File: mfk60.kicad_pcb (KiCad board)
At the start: 2 copper layers, 300 x 95.2 mm, 181 parts, among them J1 USB_C_Receptacle_USB2.0, J2 TRRS Jack, J3 ISP, J4 USB_C_Receptacle_USB2.0, J5 TRRS Jack, J6 ISP, SW1 KS-33, SW10 KS-33, SW11 KS-33, SW12 KS-33, SW13 KS-33, SW14 KS-33, SW15 KS-33, SW16 KS-33, SW17 KS-33, SW18 KS-33, SW19 KS-33, SW2 KS-33, SW20 KS-33, SW21 KS-33, SW22 KS-33, SW23 KS-33, SW24 KS-33, SW25 KS-33, SW26 KS-33, SW27 KS-33, SW28 KS-33, SW29 KS-33, SW3 KS-33, SW30 KS-33, SW31 KS-33, SW32 KS-33, SW33 KS-33, SW34 KS-33, SW35 KS-33, SW36 KS-33, SW37 KS-33, SW38 KS-33, SW39 KS-33, SW4 KS-33, SW40 KS-33, SW41 KS-33, SW42 KS-33, SW43 KS-33, SW44 KS-33, SW45 KS-33, SW46 KS-33, SW47 KS-33, SW48 KS-33, SW49 KS-33, SW5 KS-33, SW50 KS-33, SW51 KS-33, SW52 KS-33, SW53 KS-33, SW54 KS-33, SW55 KS-33, SW56 KS-33, SW57 KS-33, SW58 KS-33, SW59 KS-33, SW6 KS-33, SW60 KS-33, SW61 KS-33, SW62 RST, SW63 RST, SW7 KS-33, SW8 KS-33, SW9 KS-33, T1 Tab, T2 Tab, T3 Tab, T4 Tab, T5 Tab, T6 Tab, T7 Tab, U1 ATmega32U4-M, U2 ATmega32U4-M, Y1 16M, Y2 16M

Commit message: Adjust differential pairs
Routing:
- net USB_D-: track 17.4 -> 19.3 mm

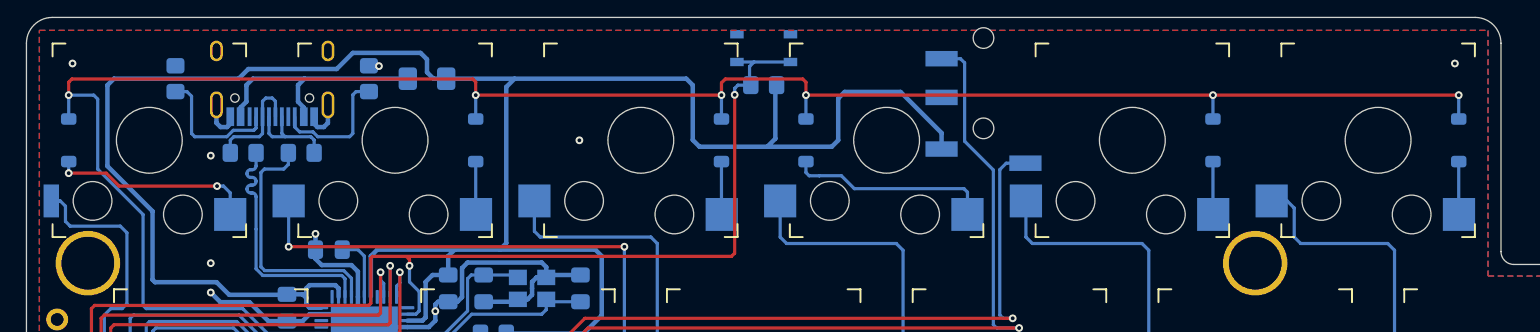
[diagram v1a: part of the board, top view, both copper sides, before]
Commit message: Minor alignment fix.
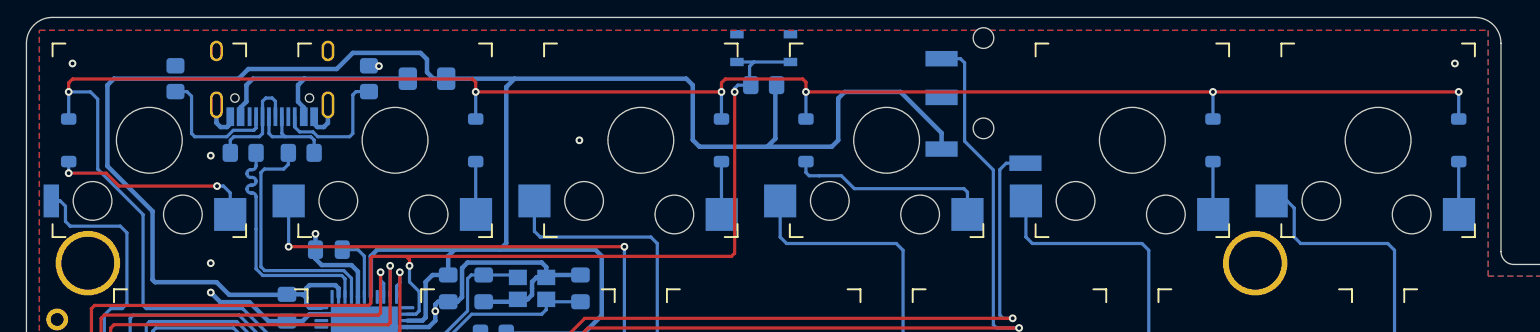
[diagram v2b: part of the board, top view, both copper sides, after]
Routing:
- net ROW1: track 157.8 -> 158.4 mm
